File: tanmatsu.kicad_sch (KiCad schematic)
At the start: 49 parts, among them J1 USB host, J10 External Add-On (SAO / PMOD), J2 Micro_SD_Card, J3 USB device, J4 Headphone, J5 Speaker, J6 CAMERA, J7 SAO, J8 Expansion I3C, J9 Internal Add-On, SW1 Boot, U1 USBLC6-2P6, U2 USBLC6-2P6, U3 CH334R, U4 USBLC6-2P6, U5 ESD, U6 ESD, Y1 12MHz

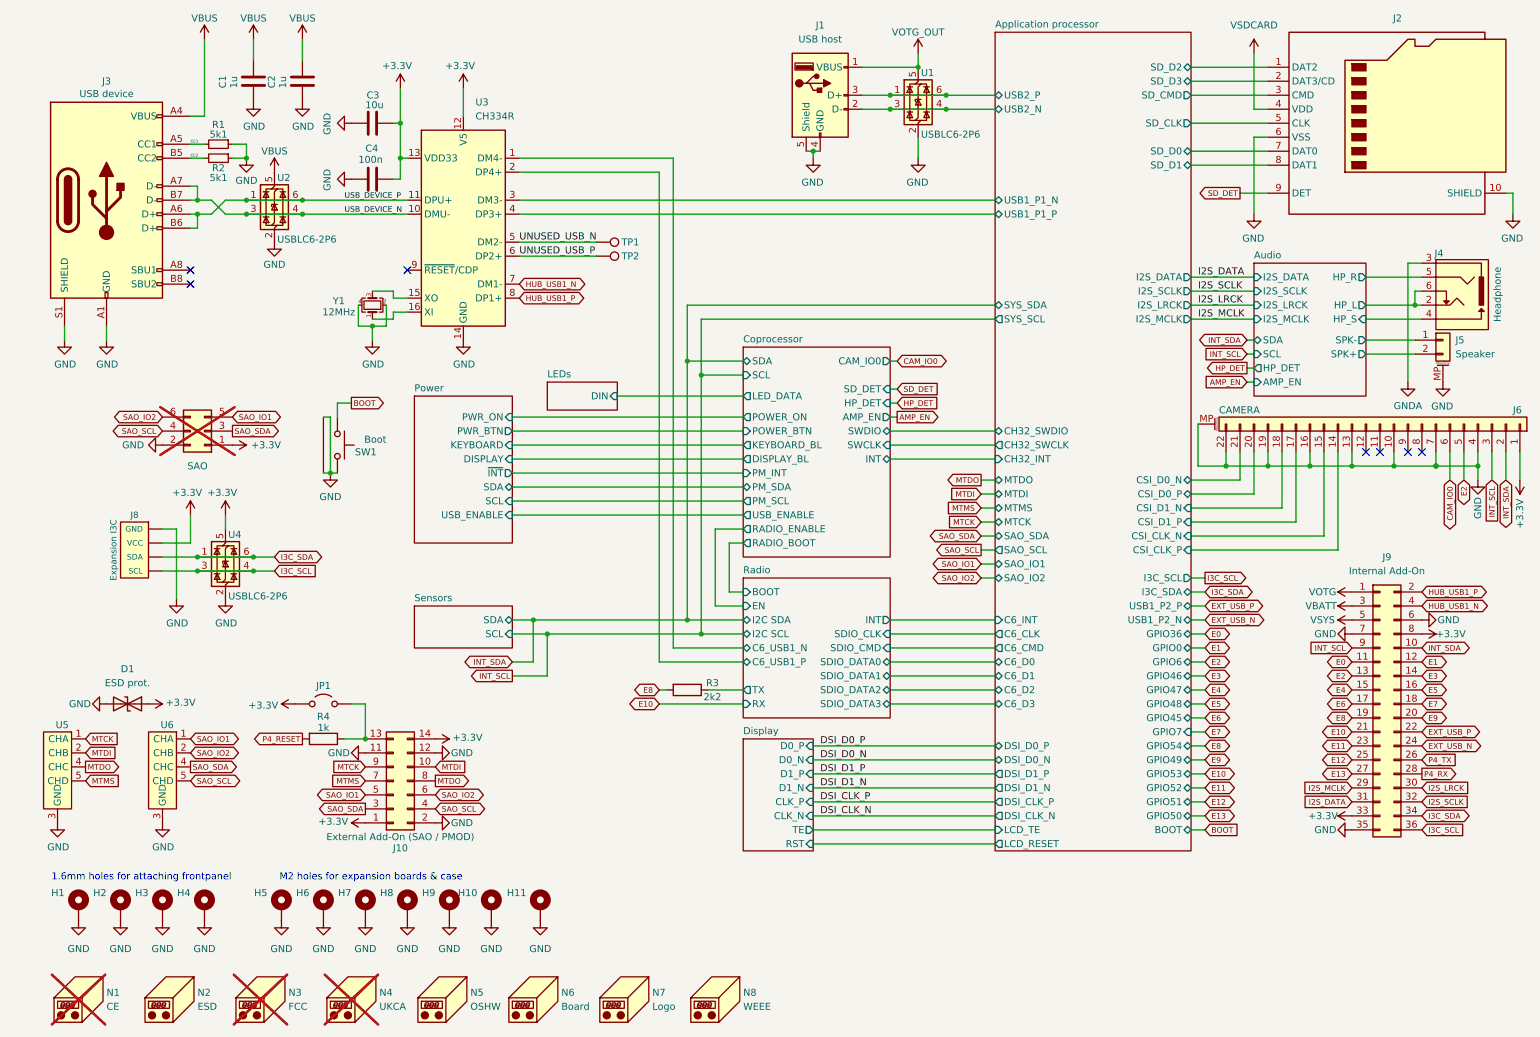
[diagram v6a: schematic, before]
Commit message: Add JLC rotation and position offsets
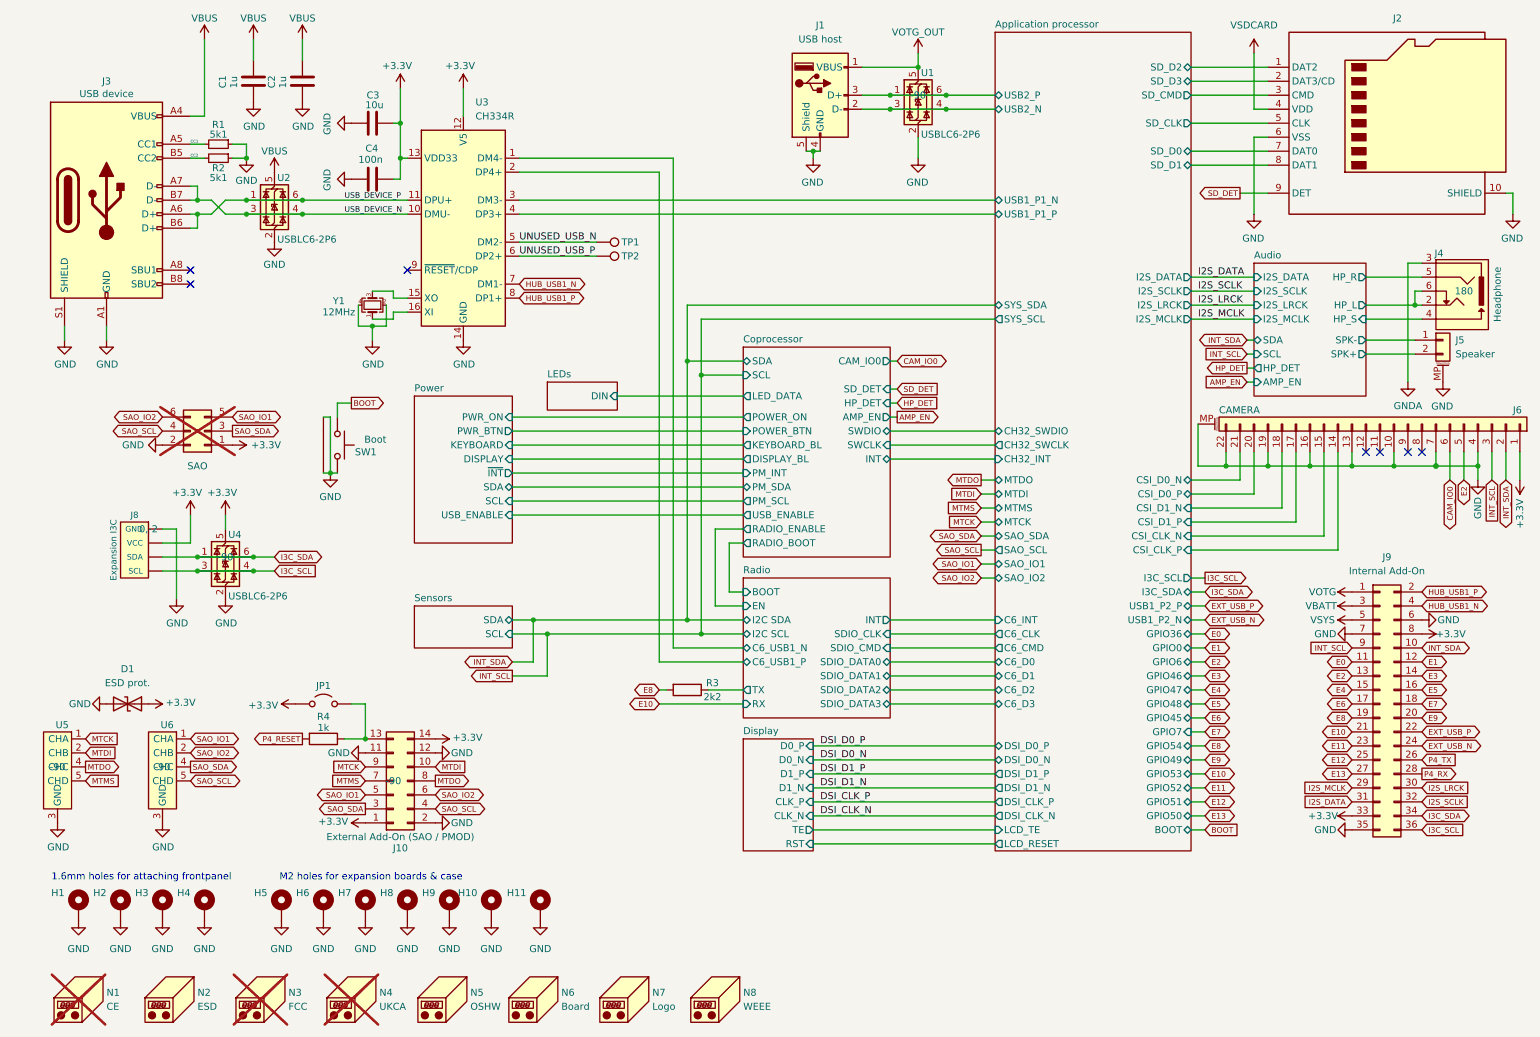
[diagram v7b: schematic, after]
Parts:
- J10: Check_pricesFT Rotation Offset (none) -> -90; FT Rotation Offset (none) -> -90
- J2, J4: FT Rotation Offset (none) -> 180
- J3: FT Position Offset (none) -> 0,1
- J8: FT Position Offset (none) -> 0,-2
- J9, U1, U2, U3, U4, U5, U6: FT Rotation Offset (none) -> -90
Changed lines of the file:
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@@
 			)
 		)
+		(property "FT Rotation Offset" "-90"
+			(at 17.78 149.86 0)
+			(effects
+				(font
+					(size 1.27 1.27)
+				)
+			)
+		)
 		(pin "8"
 		)
@@
 			)
 		)
+		(property "FT Rotation Offset" "180"
+			(at 273.05 63.5 0)
+			(effects
+				(font
+					(size 1.27 1.27)
+				)
+			)
+		)
 		(pin "2"
 		)
@@
 			)
 		)
+		(property "FT Rotation Offset" "-90"
+			(at 173.99 27.94 0)
+			(effects
+				(font
+					(size 1.27 1.27)
+				)
+			)
+		)
 		(pin "5"
 		)
@@
 			)
 		)
-		(property "Category" ""
+		(property "FT Rotation Offset" "-90"
 			(at 91.44 52.07 0)
 			(effects
@@
 			)
 		)
+		(property "FT Rotation Offset" "-90"
+			(at 36.83 149.86 0)
+			(effects
+				(font
+					(size 1.27 1.27)
+				)
+			)
+		)
 		(pin "8"
 		)
@@
 			)
 		)
-		(property "Check_prices" ""
-			(at 257.81 138.43 0)
-			(effects
-				(font
-					(size 1.27 1.27)
-				)
-				(hide yes)
-			)
-		)
-		(property "Description_1" ""
-			(at 257.81 138.43 0)
-			(effects
-				(font
-					(size 1.27 1.27)
-				)
-				(hide yes)
-			)
-		)
-		(property "Category" ""
+		(property "FT Rotation Offset" "-90"
 			(at 257.81 138.43 0)
 			(effects
@@
 			)
 		)
+		(property "FT Rotation Offset" "-90"
+			(at 48.26 111.76 0)
+			(effects
+				(font
+					(size 1.27 1.27)
+				)
+			)
+		)
 		(pin "5"
 		)
@@
 			)
 		)
-		(property "Check_prices" ""
-			(at 57.15 46.99 0)
-			(effects
-				(font
-					(size 1.27 1.27)
-				)
-				(hide yes)
-			)
-		)
-		(property "Description_1" ""
-			(at 57.15 46.99 0)
-			(effects
-				(font
-					(size 1.27 1.27)
-				)
-				(hide yes)
-			)
-		)
-		(property "Category" ""
+		(property "FT Rotation Offset" "-90"
 			(at 57.15 46.99 0)
 			(effects
@@
 			)
 		)
-		(property "Check_prices" ""
+		(property "Check_pricesFT Rotation Offset" "-90"
 			(at 78.74 152.4 0)
 			(effects
@@
 			)
 		)
-		(property "Description_1" ""
+		(property "FT Rotation Offset" "-90"
 			(at 78.74 152.4 0)
 			(effects
@@
 					(size 1.27 1.27)
 				)
-				(hide yes)
-			)
-		)
-		(property "Category" ""
-			(at 78.74 152.4 0)
-			(effects
-				(font
-					(size 1.27 1.27)
-				)
-				(hide yes)
 			)
 		)
@@
 			)
 		)
+		(property "FT Position Offset" "0,-2"
+			(at 34.29 106.68 0)
+			(effects
+				(font
+					(size 1.27 1.27)
+				)
+			)
+		)
 		(pin "1"
 		)
@@
 			)
 		)
-		(property "Check_prices" ""
-			(at 26.67 46.99 0)
-			(effects
-				(font
-					(size 1.27 1.27)
-				)
-				(hide yes)
-			)
-		)
-		(property "Description_1" ""
-			(at 26.67 46.99 0)
-			(effects
-				(font
-					(size 1.27 1.27)
-				)
-				(hide yes)
-			)
-		)
-		(property "Category" ""
+		(property "FT Position Offset" "0,1"
 			(at 26.67 46.99 0)
 			(effects
@@
 			)
 		)
-		(property "Check_prices" ""
-			(at 260.35 33.02 0)
-			(effects
-				(font
-					(size 1.27 1.27)
-				)
-				(hide yes)
-			)
-		)
-		(property "Description_1" ""
-			(at 260.35 33.02 0)
-			(effects
-				(font
-					(size 1.27 1.27)
-				)
-				(hide yes)
-			)
-		)
-		(property "Category" ""
+		(property "FT Rotation Offset" "180"
 			(at 260.35 33.02 0)
 			(effects

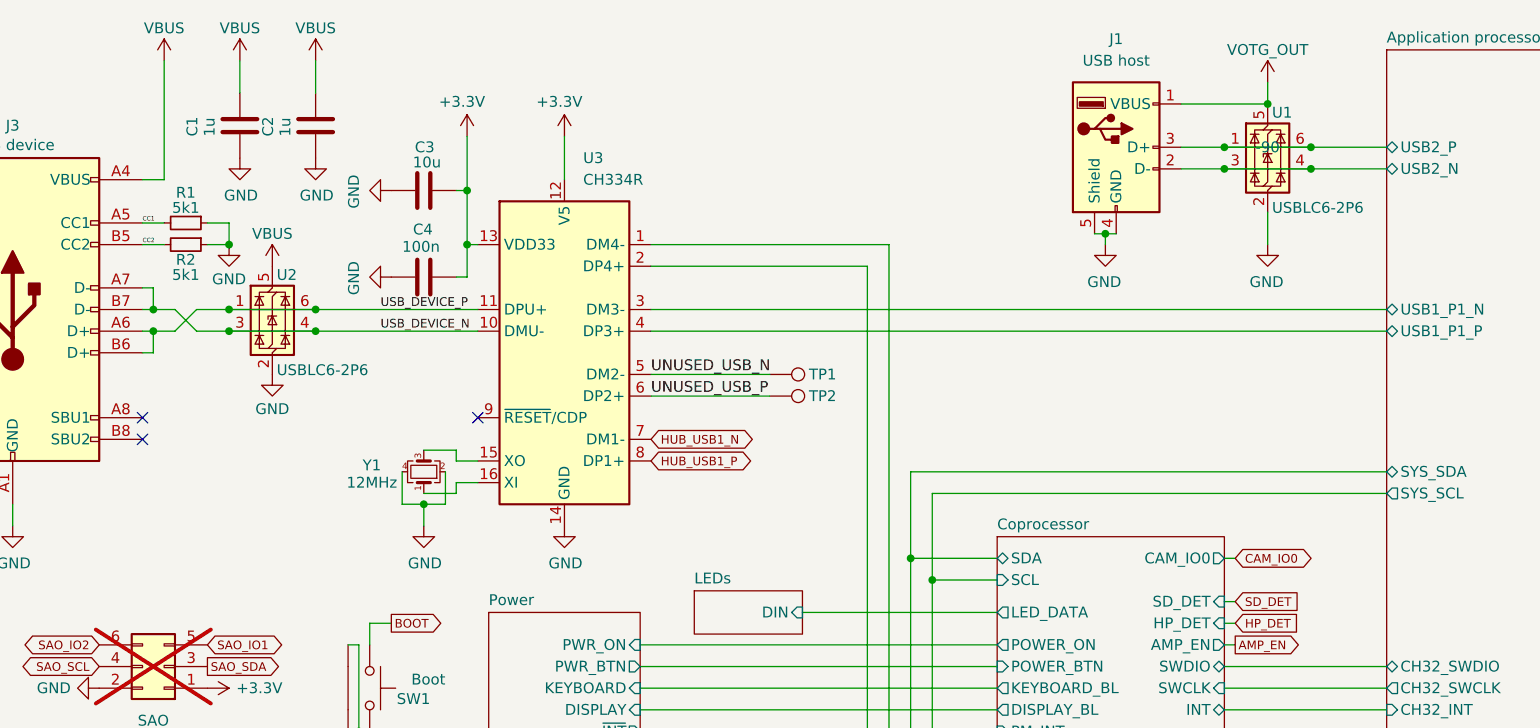
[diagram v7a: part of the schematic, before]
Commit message: Hide H6 silkscreen, replace U2 with TPD4E05U06DQAR
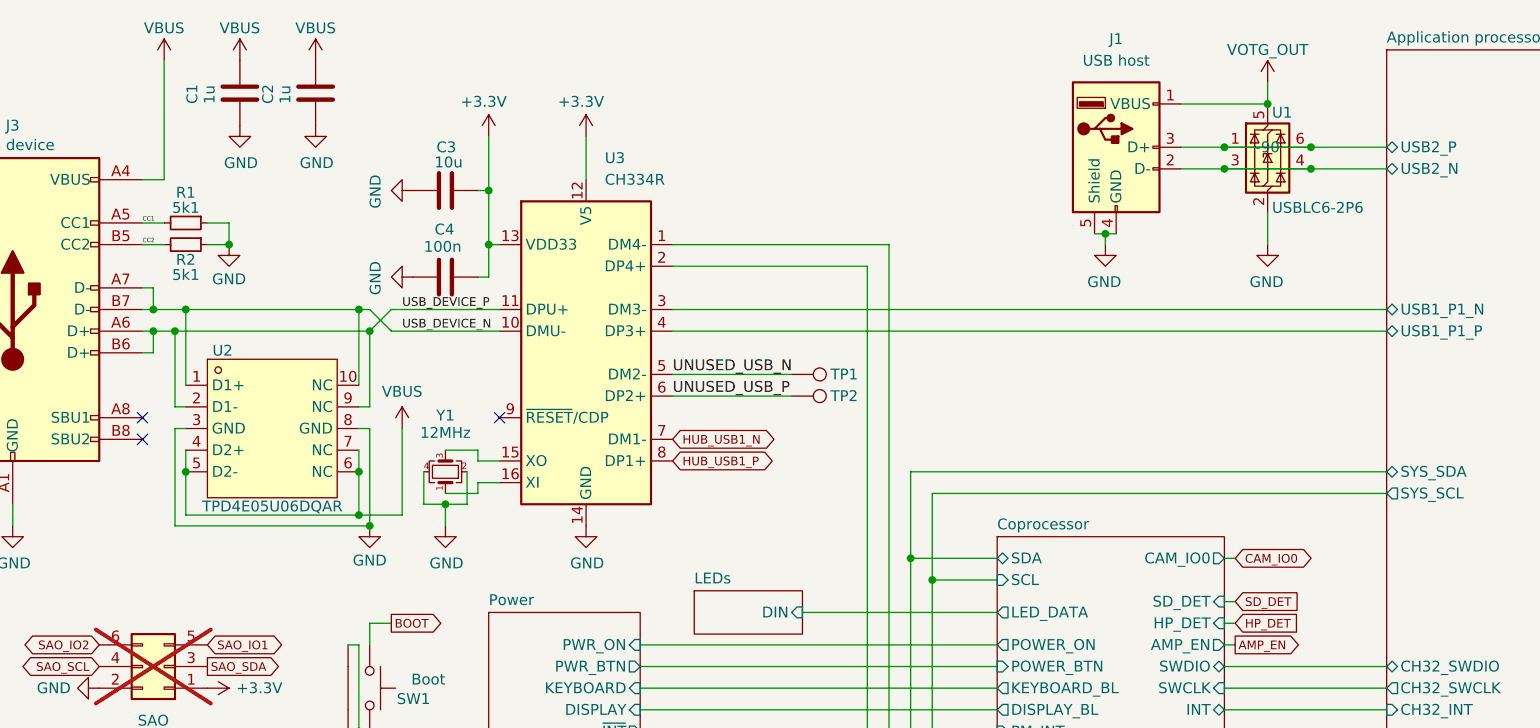
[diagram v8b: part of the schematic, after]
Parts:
- removed U2: USBLC6-2P6, Package_TO_SOT_SMD:SOT-666, symbol Power_Protection:USBLC6-2P6
- added U2: TPD4E05U06DQAR, library:USON-10_L2.5-W1.0-P0.50-BL, symbol TPD4E05U06DQAR:TPD4E05U06DQAR_C138714
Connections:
- net GND: now also U2.3 (GND), U2.8 (GND)
- net USB_DEVICE_N: now also U2.1 (D1+), U2.10 (NC)
- net USB_DEVICE_P: now also U2.2 (D1-), U2.9 (NC)
- net VBUS: now also U2.4 (D2+), U2.5 (D2-), U2.6 (NC), U2.7 (NC)
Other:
- moved on the sheet: C1, C2, C3, C4, TP1, TP2, U3, Y1
